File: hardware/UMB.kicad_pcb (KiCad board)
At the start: 6 copper layers, 128.8 x 67 mm, 228 parts, among them J1 PinHeader 02x04, J10 PH1-03-UA, J11 PH1-03-UA, J12 PH1-03-UA, J13 Conn_01x05, J14 Conn_01x05, J15 Conn_01x05, J16 Conn_01x05, J17 Conn_01x05, J18 Conn_01x05, J19 Conn_01x03, J2 PinHeader 02x04, J20 Conn_01x03, J21 Conn_01x03, J22 Conn_01x03, J23 Conn_01x03, J24 Conn_01x03, J25 Conn_01x02, J26 Conn_01x02, J27 FTSH-107-01-L-D-K, J3 PinHeader 02x04, J4 PinHeader 02x04, J5 PinHeader 02x04, J6 PinHeader 02x04, J7 PH1-03-UA, J8 PH1-03-UA, J9 PH1-03-UA, U1 STM32G0C1KCTxN, U10 LDK320ADU120R, U11 INA2128UA_1K, U12 INA2128UA_1K, U13 INA2128UA_1K, U14 TLC274AIDR, U15 TLC274AIDR, U16 TLC274AIDR, U2 ADS114S08BIPBSR, U3 ADM3057ExRW, U4 TPS563300DRLR, U5 TPS563219ADDFR, U6 LM2940SX-12_NOPB, U7 LM1117IMP-5.0, U8 TLV743P, U9 AP2127N3-1.5

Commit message: Added description, fixed engineering fee
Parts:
- removed the ? at (149.2, 93.8)
- removed the ? at (56.3, 112.5)
- removed the ? at (114.7, 92.7)
- removed the ? at (133.8, 92.7)
- removed the ? at (145.3, 93.8)
- removed the ? at (127.0, 92.7)
- removed the ? at (100.7, 92.7)
- removed the ? at (139.2, 92.7)
- removed the ? at (151.8, 93.0)
- removed the ? at (62.2, 92.7)
- removed the ? at (95.4, 92.7)
- removed the ? at (58.4, 92.6)
- removed the ? at (76.2, 92.7)
- removed the ? at (56.3, 117.8)
- removed the ? at (81.4, 92.7)
- moved R13 1.60 mm to (172.3, 139.4)
- moved R12 1.32 mm to (172.3, 142.7), turned to 90 degrees
- moved C21 0.52 mm to (171.4, 137.0)
- renumbered TP20 to 20, TP21 to 21, TP22 to 22, TP23 to 23, TP24 to 24, TP25 to 25, TP26 to 26, TP27 to 27, TP28 to 28, TP29 to 29, TP30 to 30, TP31 to 31, TP34 to 34, TP37 to 37, TP9 to 9
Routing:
- net +7V: track 36.9 -> 38.6 mm
- net Net-(U5-VFB): track 10.9 -> 10.3 mm
- net Net-(U5-VIN): vias 21 -> 36
- net +12V: vias 8 -> 23
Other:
- rule pad_to_mask_clearance: 0.038 -> 0
- board text added: "100"
- board text added: "1k"
- board text added: "25"
- board text added: "3 pin input:"
- board text added: "5"
- board text added: "5 pin input:"
- board text added: "GND D 5V"
- board text added: "GND S+ S- 5V 12V"
- board text added: "for 12V"
- board text added: "for 5V"
- board text added: "gain:"

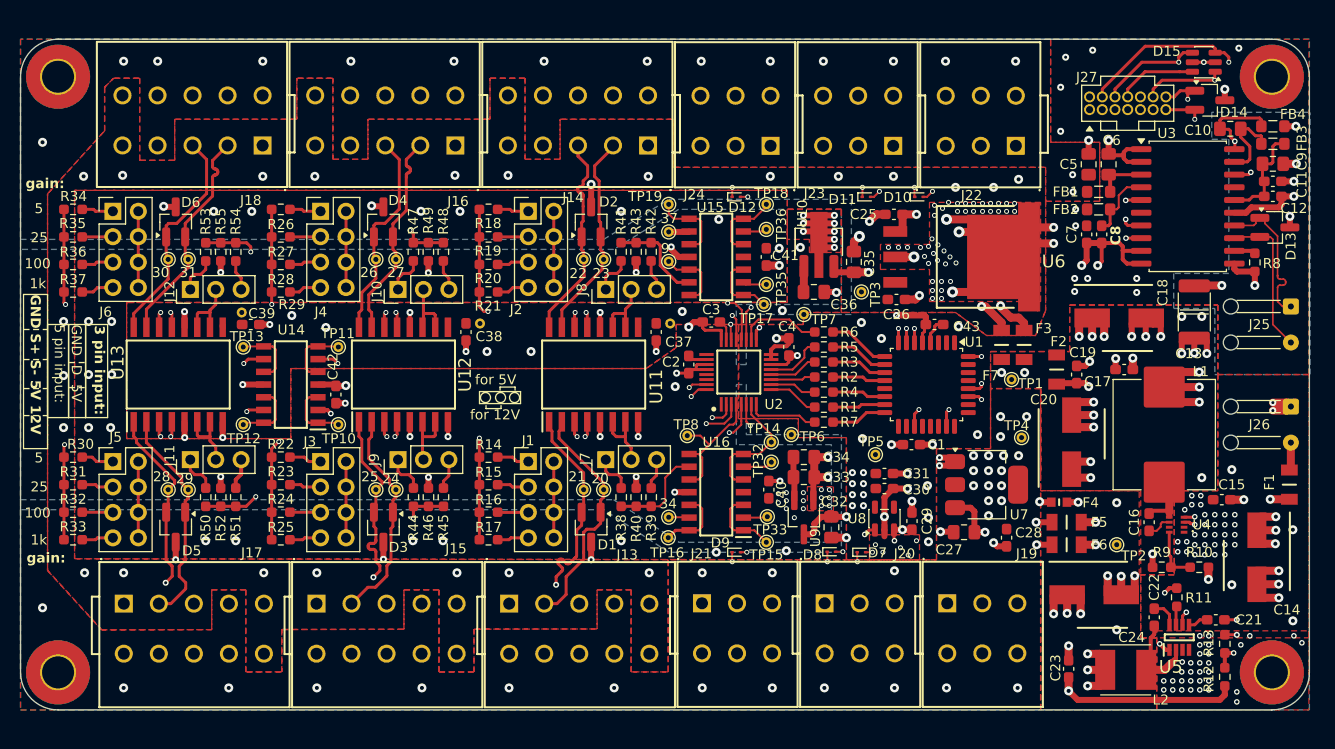
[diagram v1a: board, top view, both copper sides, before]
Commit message: Vias on pad and traces under components fix
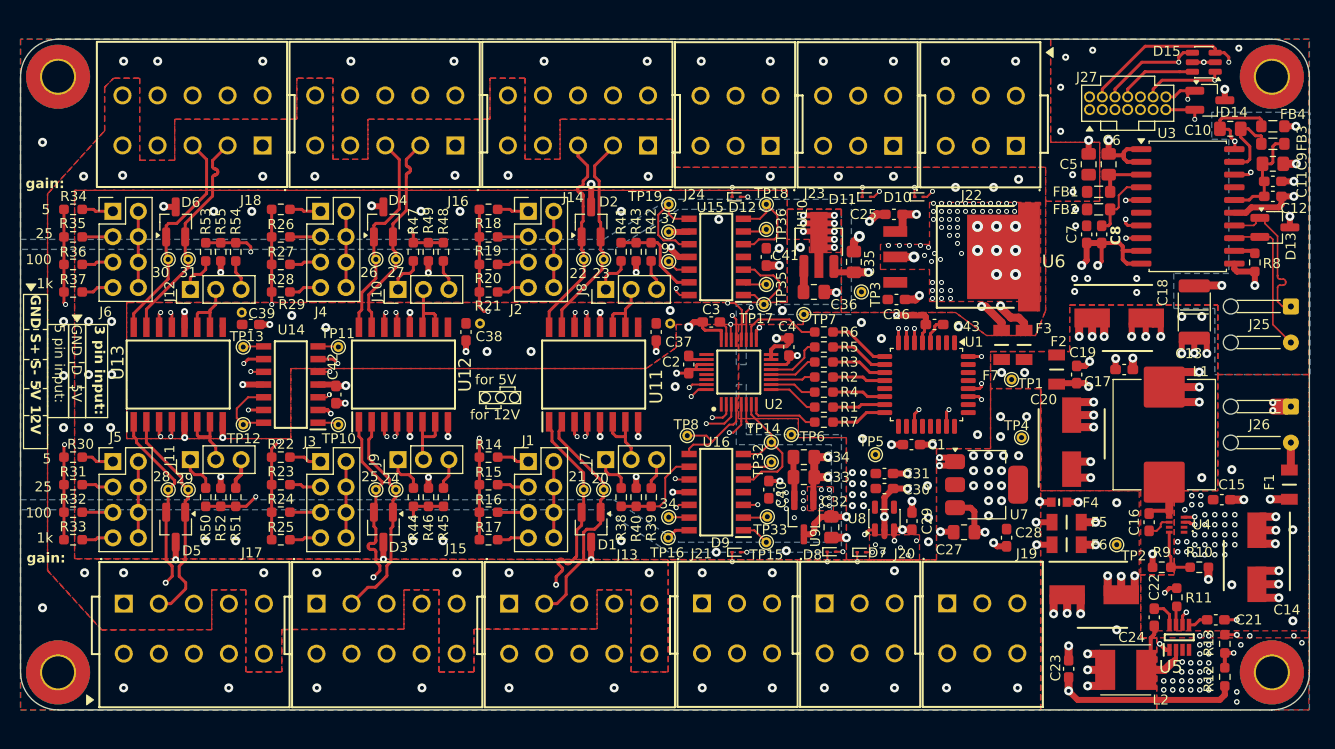
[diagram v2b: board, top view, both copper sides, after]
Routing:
- net GND: track 212.4 -> 197.1 mm, vias 157 -> 168
- net /ADC/DIF1: track 15.0 -> 18.3 mm, vias 0 -> 1
- net /ADC/SE2: track 22.1 -> 18.8 mm, vias 1 -> 2
- net /ADC/SE5: track 25.0 -> 28.0 mm
- net /ADC/SE3: track 24.9 -> 22.0 mm, vias 1 -> 2
- net /ADC/SE6: track 25.6 -> 28.5 mm
- net /ADC/SE1: track 13.0 -> 15.6 mm
- net /ADC/SE4: track 11.9 -> 14.3 mm
- net /ADC/DIF2: track 18.7 -> 17.5 mm, vias 1 -> 2
- net /ADC/DIF4: track 55.4 -> 54.8 mm, vias 1 -> 2
- net /ADC/DIF6: track 62.8 -> 62.3 mm, vias 1 -> 2
- net /ADC/DIF3: track 48.9 -> 49.0 mm, vias 1 -> 2
